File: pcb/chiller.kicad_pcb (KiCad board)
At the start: 2 copper layers, 41 parts, among them J1 CONN_01X03, J10 CONN_01X03, J11 CONN_01X02, J2 CONN_01X03, J3 CONN_01X03, J4 CONN_01X02, J5 CONN_01X02, J6 CONN_01X02, J7 CONN_01X02, J8 CONN_01X02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

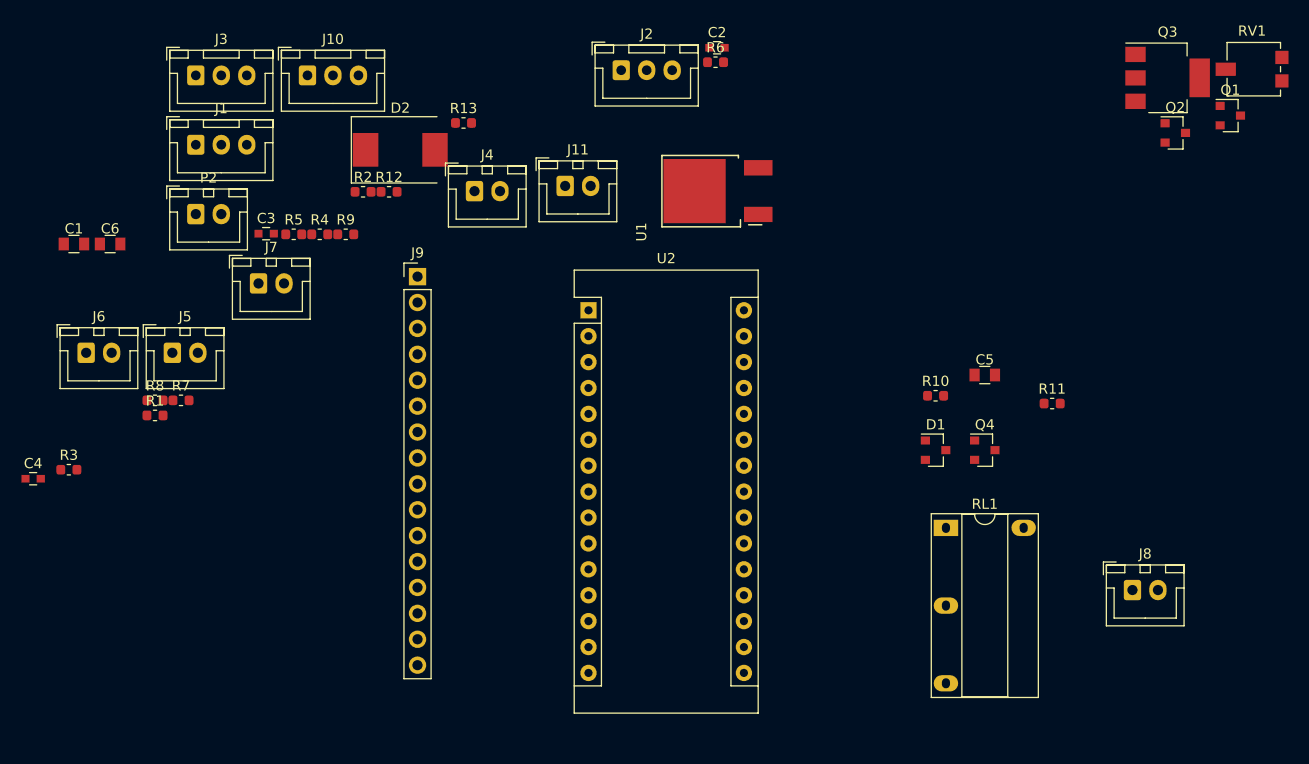
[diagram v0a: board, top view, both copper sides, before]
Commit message: Fix footprints, place all components.
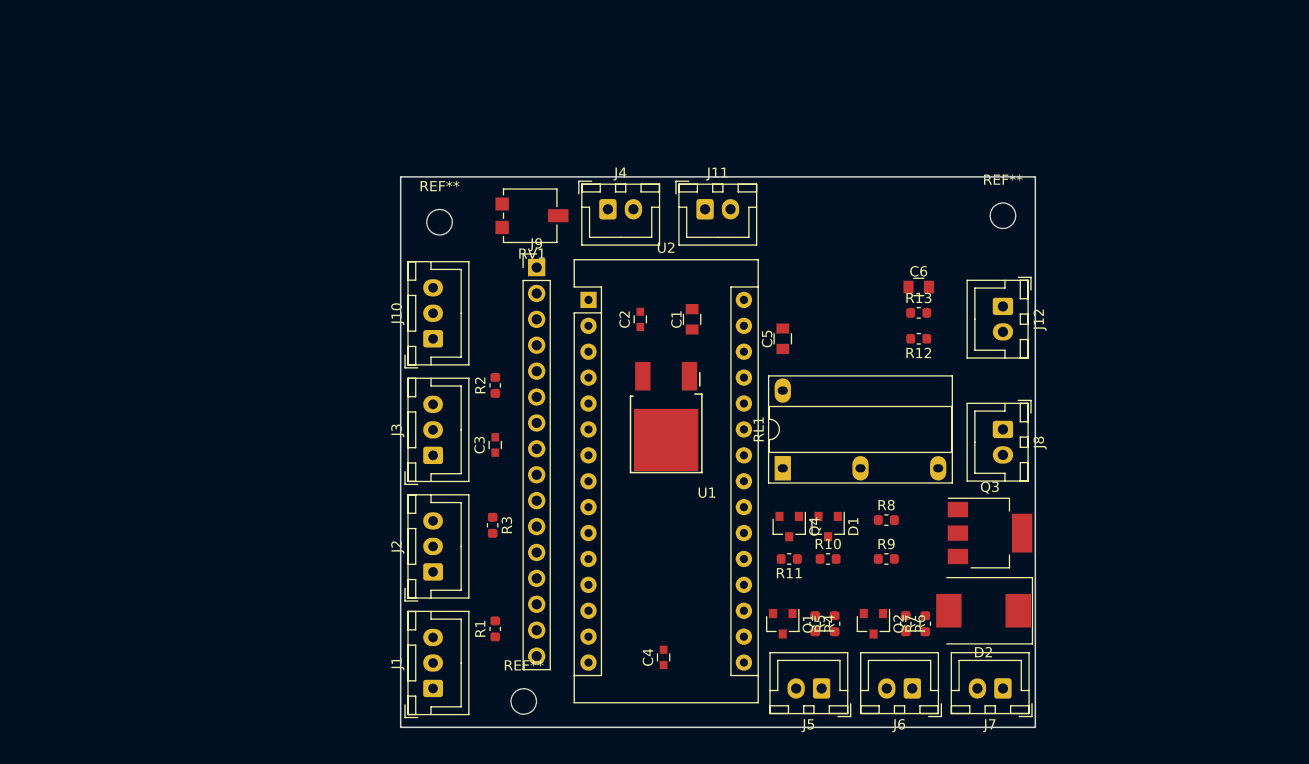
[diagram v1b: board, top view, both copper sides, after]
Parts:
- removed P2: CONN_01X02, Connector_JST:JST_XH_B02B-XH-A_1x02_P2.50mm_Vertical
- added J12: CONN_01X02, Connector_JST:JST_XH_B02B-XH-A_1x02_P2.50mm_Vertical, F.Cu at (238.8, 61.6)
- added REF**: MountingHole_2.5mm, MountingHole:MountingHole_2.5mm, F.Cu at (183.5, 53.3)
- added REF**: MountingHole_2.5mm, MountingHole:MountingHole_2.5mm, F.Cu at (191.8, 100.3)
- added REF**: MountingHole_2.5mm, MountingHole:MountingHole_2.5mm, F.Cu at (238.8, 52.7)
- R11: value R -> 10K
- RL1: value G6B-1114C-US-DC5 -> G6B-1114C-US5DC; footprint libs:DIL-relay -> modules:DIL-relay
- U1: footprint libs:DPAK-3 -> modules:DPAK-3
- moved J6 87.4 mm to (229.9, 99.1), turned to 180 degrees
- moved J7 83.1 mm to (238.8, 99.1), turned to 180 degrees
- moved C6 79.4 mm to (230.5, 59.7)
- moved R7 76.2 mm to (231.1, 92.7), turned to 90 degrees
- moved D2 72.9 mm to (236.9, 91.4), turned to 180 degrees
- moved R8 72.7 mm to (227.3, 82.5)
- moved RV1 72.4 mm to (192.4, 52.7), turned to 180 degrees
- moved J5 71.7 mm to (221.0, 99.1), turned to 180 degrees
- moved Q1 66.4 mm to (217.2, 92.7), turned to 270 degrees
- moved R5 65.3 mm to (222.2, 92.7), turned to 90 degrees
- moved C4 64.3 mm to (205.5, 96.0), turned to 90 degrees
- moved R9 61.8 mm to (227.3, 86.4)
- moved R4 61.8 mm to (220.3, 92.7), turned to 270 degrees
- moved C1 61.1 mm to (208.3, 62.9), turned to 90 degrees
- moved J1 58.2 mm to (182.9, 99.1), turned to 90 degrees
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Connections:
- J8 pad 1: (no net) -> Net-(J8-Pad1)
- J8 pad 2: (no net) -> Net-(J8-Pad2)
- RL1 pad 1: (no net) -> Net-(D1-Pad1)
- RL1 pad 2: (no net) -> +5V
- RL1 pad 3: (no net) -> Net-(J8-Pad2)
- RL1 pad 4: (no net) -> Net-(J8-Pad1)
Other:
- board outline added: 62.2 x 54 mm

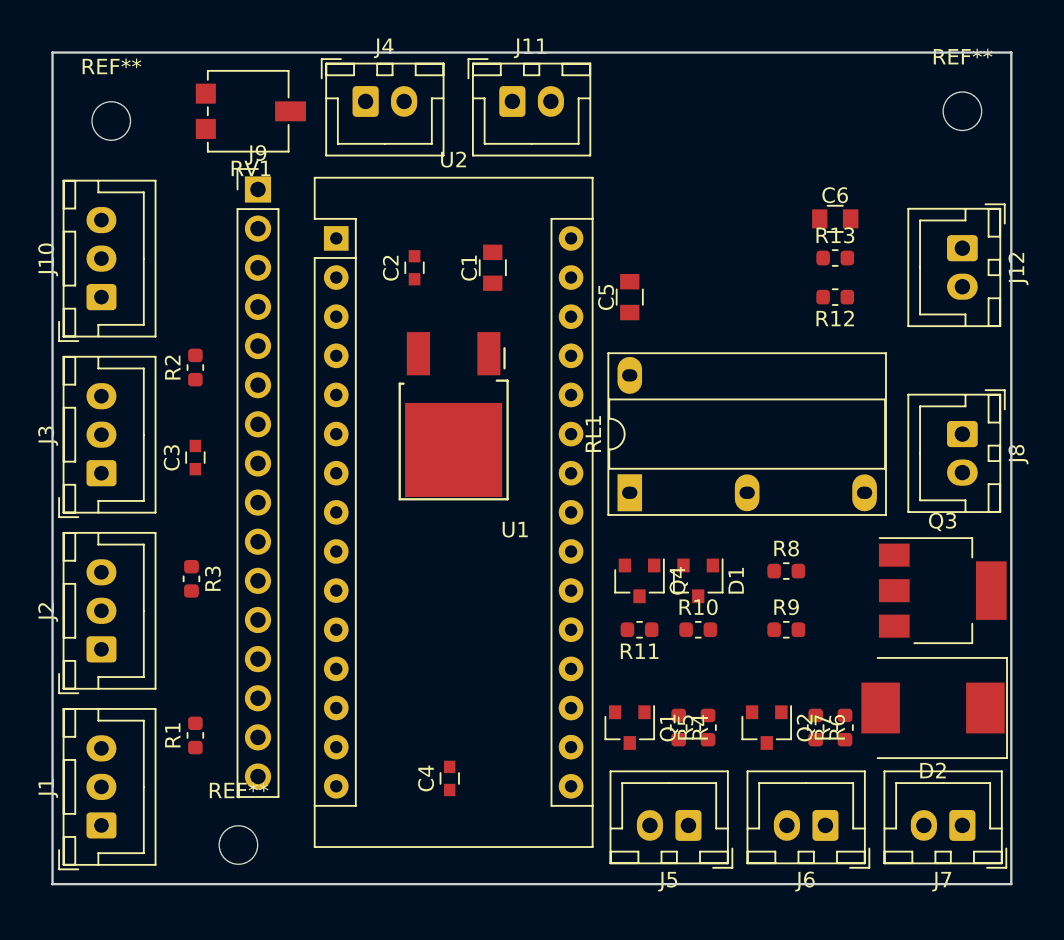
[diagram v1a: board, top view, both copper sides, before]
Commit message: Complete routing.
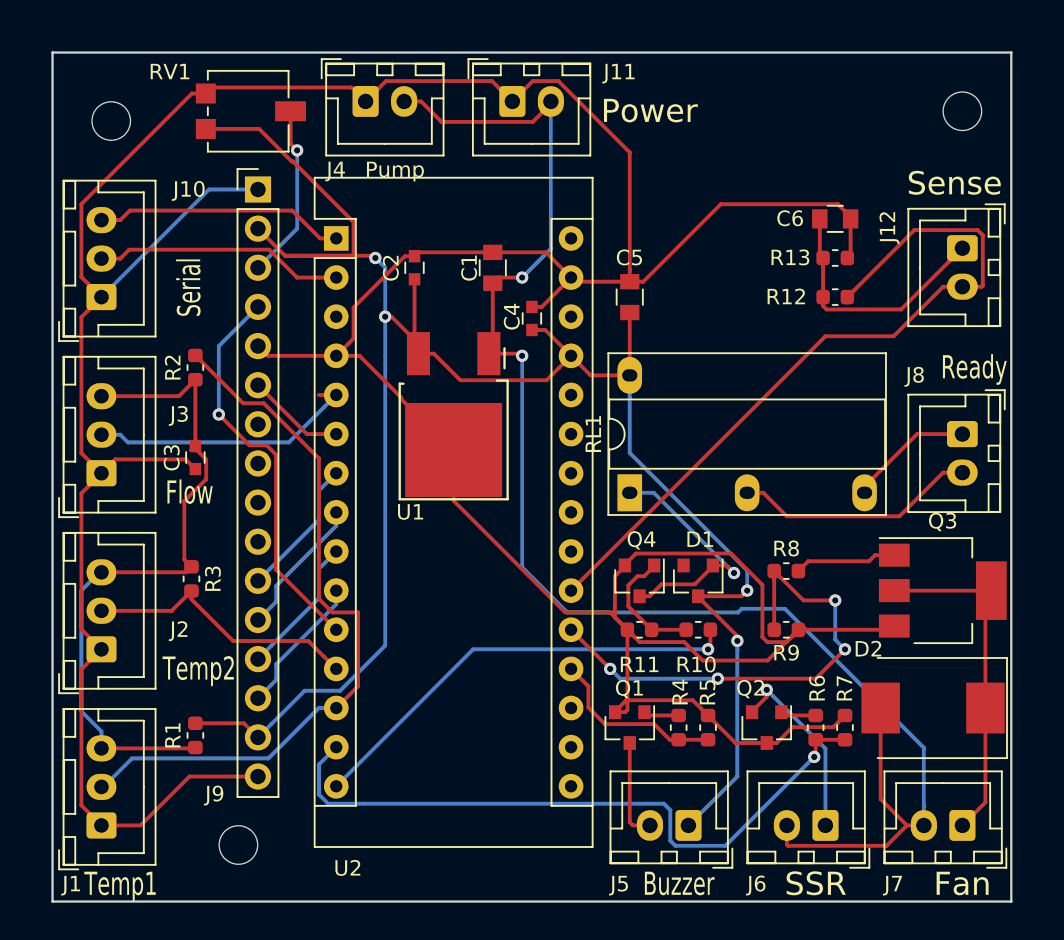
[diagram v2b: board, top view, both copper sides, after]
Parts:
- J9: value LCD-20X4 -> LCD
- moved C4 30.3 mm to (210.8, 66.2), turned to 270 degrees
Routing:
- net GND: track 0.00 -> 269.5 mm
- net +5V: track 0.00 -> 136.8 mm, vias 0 -> 4
- net +12V: track 0.00 -> 100.8 mm, vias 0 -> 2
- net A2: track 0.00 -> 48.9 mm
- net D10: track 0.00 -> 47.0 mm
- net Net-(C3-Pad2): track 0.00 -> 44.8 mm
- net D11: track 0.00 -> 43.7 mm, vias 0 -> 1
- net A1: track 0.00 -> 31.9 mm, vias 0 -> 4
- net D12: track 0.00 -> 29.1 mm, vias 0 -> 1
- net Net-(J9-Pad4): track 0.00 -> 25.8 mm, vias 0 -> 1
- net Net-(D2-Pad1): track 0.00 -> 22.3 mm
- net D9: track 0.00 -> 18.2 mm
- net D2: track 0.00 -> 18.0 mm
- net Net-(C6-Pad1): track 0.00 -> 16.5 mm
- net TX: track 0.00 -> 16.2 mm
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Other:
- board size 62.2 x 54 mm -> 62.2 x 55.1 mm
- board text added: "Buzzer"
- board text added: "Fan"
- board text added: "Flow"
- board text added: "Power"
- board text added: "Pump"
- board text added: "Ready"
- board text added: "SSR"
- board text added: "Sense"
- board text added: "Serial"
- board text added: "Temp1"
- board text added: "Temp2"

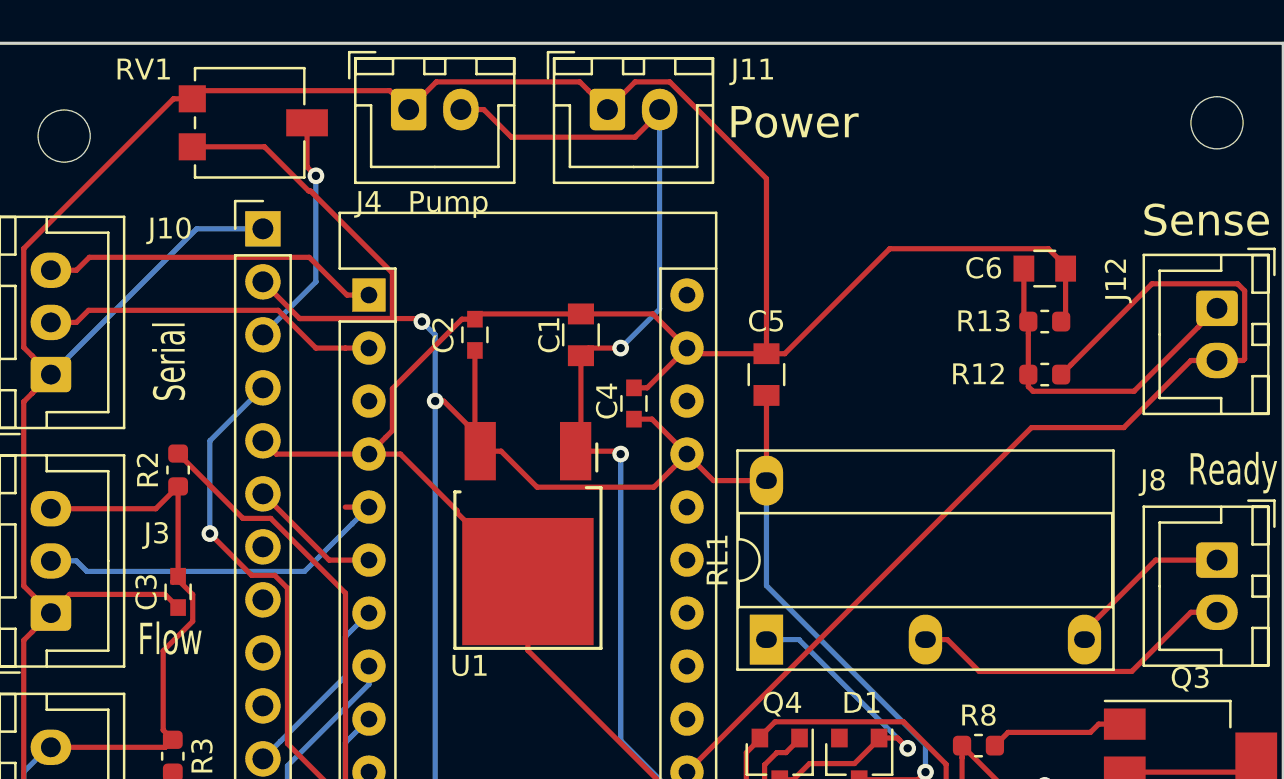
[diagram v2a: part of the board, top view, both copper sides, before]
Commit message: Make pretty.
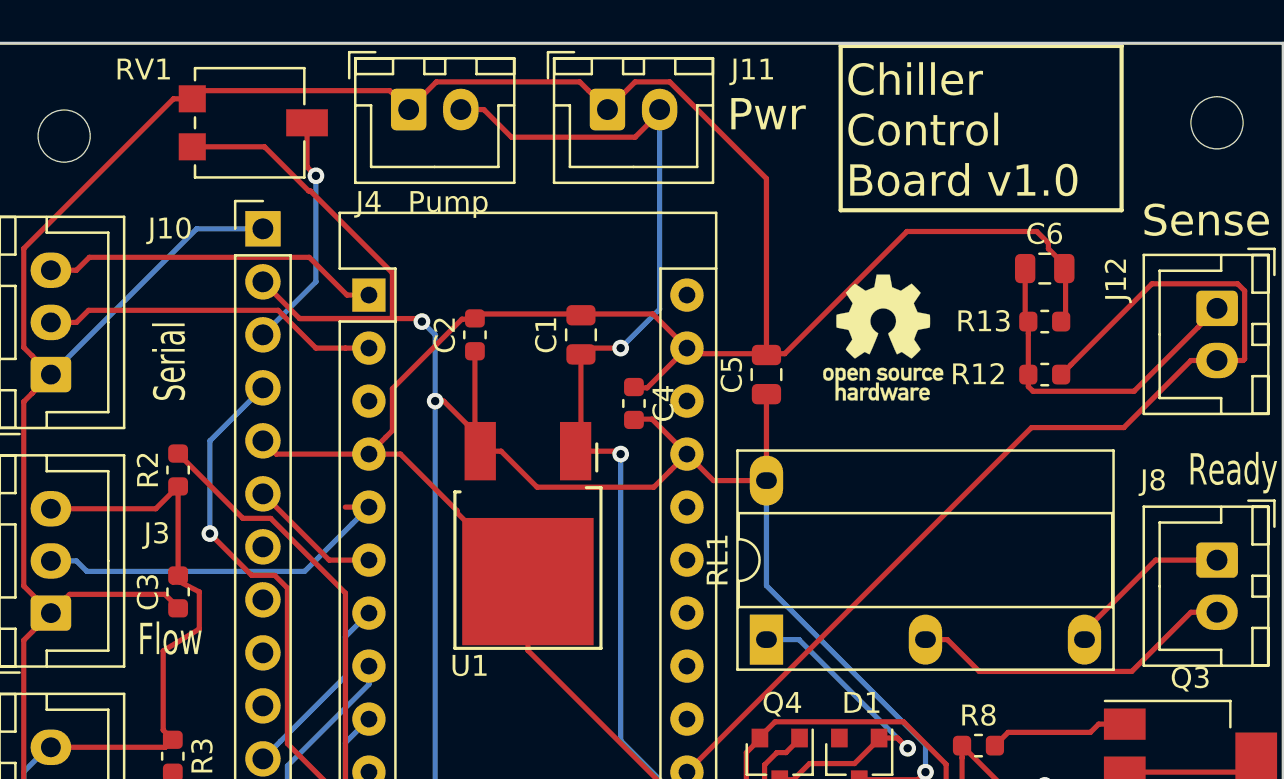
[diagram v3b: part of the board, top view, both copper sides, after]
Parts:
- added REF**: OSHW-Logo_5.7x6mm_SilkScreen, Symbol:OSHW-Logo_5.7x6mm_SilkScreen, F.Cu at (222.8, 63.0)
- C1, C5, C6: footprint Capacitors_SMD:C_0805 -> Capacitor_SMD:C_0805_2012Metric
- C2, C3, C4: footprint Capacitors_SMD:C_0603 -> Capacitor_SMD:C_0603_1608Metric
- D2: footprint Diodes_SMD:D_SMC -> Diode_SMD:D_SMC
- J9: value LCD -> LCD-20X4
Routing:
- net GND: track 269.5 -> 270.3 mm
- net Net-(C3-Pad2): track 44.8 -> 45.5 mm
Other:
- board text added: "Chiller Control Board v1.0"
- board text added: "Pwr"
- board text added: "https://github.com/bullestock/chiller"
- board text removed: "Power"
